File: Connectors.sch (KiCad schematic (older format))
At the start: 9 parts, among them J1 SM08B-CPTK-1A-TBL, J10 Conn_01x04, J17 Conn_01x04, J2 Conn_02x20_Odd_Even, J3 SM02B-CPTK-1A-TB, J5 BM02B-CPTK-1A-TB, J6 BM50B-SHLDS-G-TFT, J7 SM08B-CPTK-1A-TB, J8 BM08B-CPTK-1A-TB

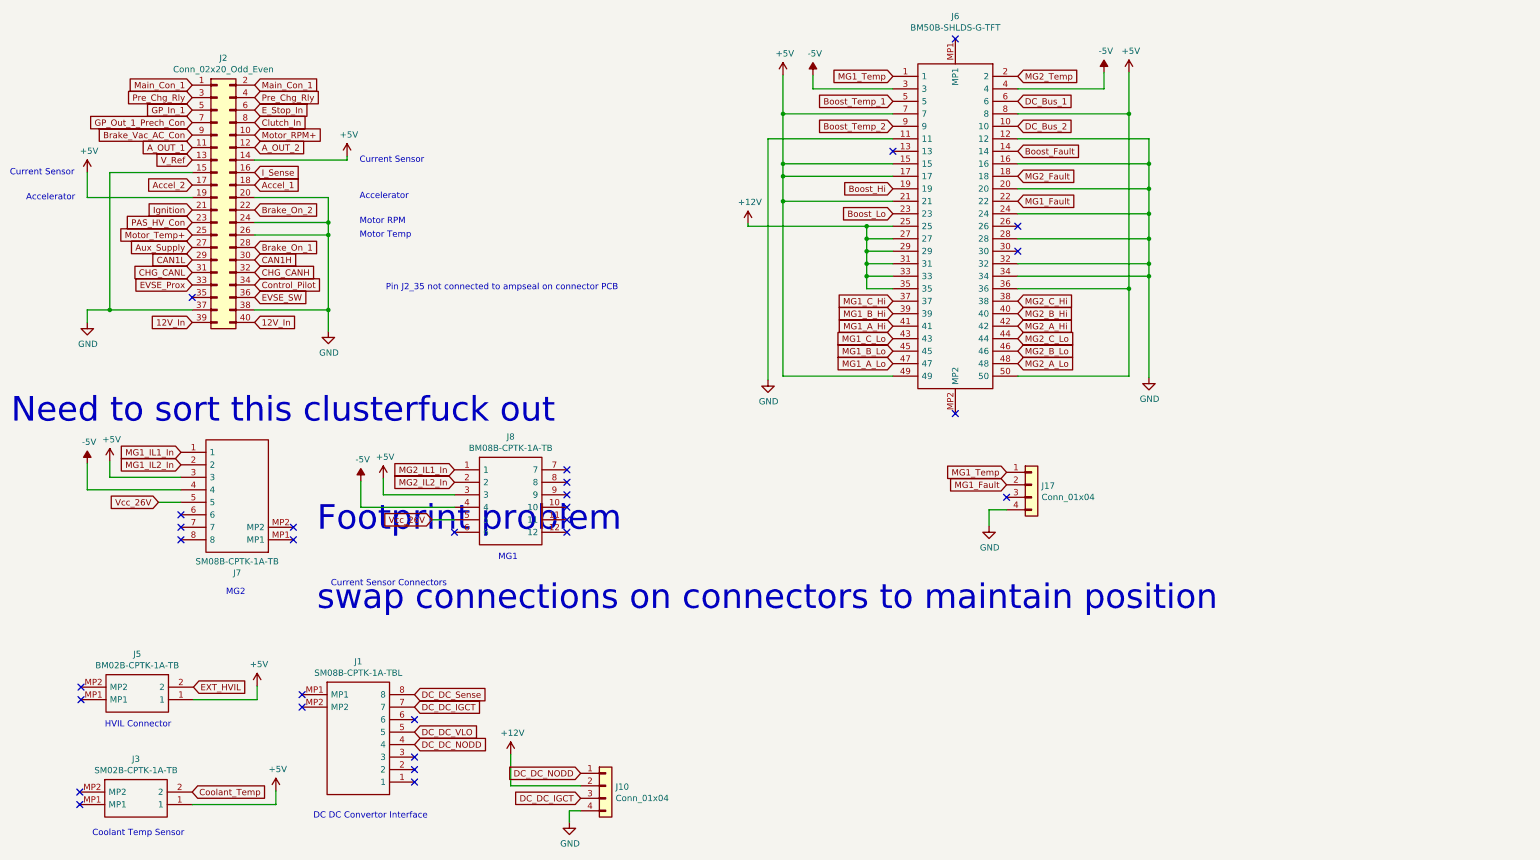
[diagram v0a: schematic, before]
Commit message: corrected tracking error around MG1 and MG current sensors.  J7 footprint updated (J1 left unchanged as tracking layout is currently ok).
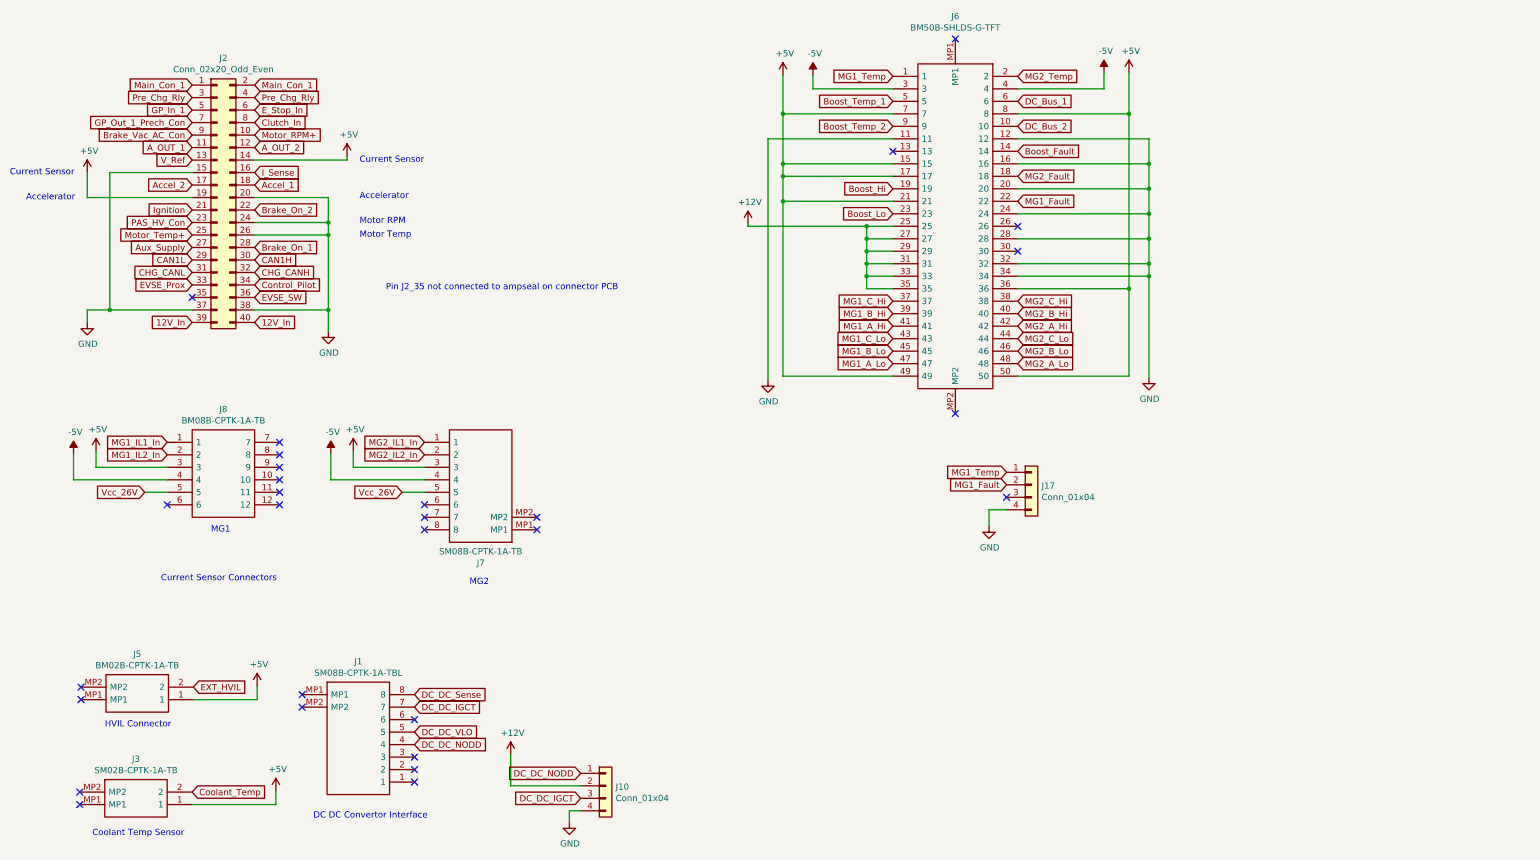
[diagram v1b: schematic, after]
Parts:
- J7: footprint SamacSys_Parts:SM08BCPTK1ATBL -> SamacSys_Parts:SM08BCPTK1ATBL_odd_even
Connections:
- net MG1_IL1_In: now also J8.1; no longer J7.1
- net MG1_IL2_In: now also J8.2; no longer J7.2
- net MG2_IL1_In: now also J7.1; no longer J8.1
- net MG2_IL2_In: now also J7.2; no longer J8.2
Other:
- note removed: "Footprint problem\n\nswap connections on connectors to maintain position"
- note removed: "Need to sort this clusterfuck out"
- moved on the sheet: J7, J8
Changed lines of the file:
@@
 Sheet 6 8
 Title "DC Controller STM32"
-Date "2020-07-04"
-Rev "2"
+Date "2020-10-18"
+Rev "3"
 Comp ""
 Comment1 "Designed: A Martell"
@@
 L SamacSys_Parts:SM08B-CPTK-1A-TBL J7
 U 1 1 5F32A5F1
-P 3060 4870
-F 0 "J7" H 3510 5135 50  0000 C CNN
-F 1 "SM08B-CPTK-1A-TB" H 3510 5044 50  0000 C CNN
-F 2 "SamacSys_Parts:SM08BCPTK1ATBL" H 3810 4970 50  0001 L CNN
-F 3 "http://www.jst-mfg.com/product/pdf/eng/eCPT.pdf" H 3810 4870 50  0001 L CNN
-F 4 "Header Top 8 Double CPT" H 3810 4770 50  0001 L CNN "Description"
-F 5 "12" H 3810 4670 50  0001 L CNN "Height"
-F 6 "" H 3810 4570 50  0001 L CNN "Mouser Part Number"
-F 7 "" H 3810 4470 50  0001 L CNN "Mouser Price/Stock"
-F 8 "JST (JAPAN SOLDERLESS TERMINALS)" H 3810 4370 50  0001 L CNN "Manufacturer_Name"
-F 9 "SM08B-CPTK-1A-TB" H 3810 4270 50  0001 L CNN "Manufacturer_Part_Number"
-	1    3060 4870
+P 5010 4790
+F 0 "J7" H 5460 5055 50  0000 C CNN
+F 1 "SM08B-CPTK-1A-TB" H 5460 4964 50  0000 C CNN
+F 2 "SamacSys_Parts:SM08BCPTK1ATBL_odd_even" H 5760 4890 50  0001 L CNN
+F 3 "http://www.jst-mfg.com/product/pdf/eng/eCPT.pdf" H 5760 4790 50  0001 L CNN
+F 4 "Header Top 8 Double CPT" H 5760 4690 50  0001 L CNN "Description"
+F 5 "12" H 5760 4590 50  0001 L CNN "Height"
+F 6 "" H 5760 4490 50  0001 L CNN "Mouser Part Number"
+F 7 "" H 5760 4390 50  0001 L CNN "Mouser Price/Stock"
+F 8 "JST (JAPAN SOLDERLESS TERMINALS)" H 5760 4290 50  0001 L CNN "Manufacturer_Name"
+F 9 "SM08B-CPTK-1A-TB" H 5760 4190 50  0001 L CNN "Manufacturer_Part_Number"
+	1    5010 4790
 	-1   0    0    1
 $EndComp
@@
 Text GLabel 2250 6890 2    50   Input ~ 0
 Coolant_Temp
-NoConn ~ 2160 4670
-NoConn ~ 3060 4870
-NoConn ~ 3060 4770
-NoConn ~ 2160 4870
-NoConn ~ 2160 4770
-NoConn ~ 4350 4810
-Text Notes 3360 5250 0    50   ~ 0
+NoConn ~ 4110 4590
+NoConn ~ 5010 4790
+NoConn ~ 5010 4690
+NoConn ~ 4110 4790
+NoConn ~ 4110 4690
+NoConn ~ 2050 4590
+Text Notes 2000 5210 0    50   ~ 0
 Current Sensor Connectors
 $Comp
@@
 Text GLabel 2250 2730 0    50   Input ~ 0
 CHG_CANL
-Text Notes 4700 5040 0    50   ~ 0
+Text Notes 2400 4820 0    50   ~ 0
 MG1
-Text Notes 2520 5320 0    50   ~ 0
+Text Notes 4470 5240 0    50   ~ 0
 MG2
-Text GLabel 2160 4170 0    50   Input ~ 0
+Text GLabel 2050 4090 0    50   Input ~ 0
 MG1_IL1_In
-Text GLabel 2160 4270 0    50   Input ~ 0
+Text GLabel 2050 4190 0    50   Input ~ 0
 MG1_IL2_In
 $Comp
 L power:+5V #PWR?
 U 1 1 5F14A7F7
-P 1590 4240
+P 3540 4160
 AR Path="/5F14A7F7" Ref="#PWR?"  Part="1"
 AR Path="/5EDFAF50/5F14A7F7" Ref="#PWR083"  Part="1"
-F 0 "#PWR083" H 1590 4090 50  0001 C CNN
-F 1 "+5V" H 1605 4413 50  0000 C CNN
-F 2 "" H 1590 4240 50  0001 C CNN
-F 3 "" H 1590 4240 50  0001 C CNN
-	1    1590 4240
+F 0 "#PWR083" H 3540 4010 50  0001 C CNN
+F 1 "+5V" H 3555 4333 50  0000 C CNN
+F 2 "" H 3540 4160 50  0001 C CNN
+F 3 "" H 3540 4160 50  0001 C CNN
+	1    3540 4160
 	1    0    0    -1
 $EndComp
@@
 L power:-5V #PWR?
 U 1 1 5F14DDA6
-P 1410 4260
+P 3360 4180
 AR Path="/5F8738CC/5F14DDA6" Ref="#PWR?"  Part="1"
 AR Path="/5EDFAF50/5F14DDA6" Ref="#PWR082"  Part="1"
-F 0 "#PWR082" H 1410 4360 50  0001 C CNN
-F 1 "-5V" H 1425 4433 50  0000 C CNN
-F 2 "" H 1410 4260 50  0001 C CNN
-F 3 "" H 1410 4260 50  0001 C CNN
-	1    1410 4260
-	1    0    0    -1
-$EndComp
-Text GLabel 1980 4570 0    50   Input ~ 0
+F 0 "#PWR082" H 3360 4280 50  0001 C CNN
+F 1 "-5V" H 3375 4353 50  0000 C CNN
+F 2 "" H 3360 4180 50  0001 C CNN
+F 3 "" H 3360 4180 50  0001 C CNN
+	1    3360 4180
+	1    0    0    -1
+$EndComp
+Text GLabel 3930 4490 0    50   Input ~ 0
 Vcc_26V
 Wire Wire Line
-	1980 4570 2160 4570
-Wire Wire Line
-	2160 4370 1590 4370
-Wire Wire Line
-	1590 4240 1590 4370
-Wire Wire Line
-	2160 4470 1410 4470
-Wire Wire Line
-	1410 4260 1410 4470
-Text GLabel 4350 4310 0    50   Input ~ 0
+	3930 4490 4110 4490
+Wire Wire Line
+	4110 4290 3540 4290
+Wire Wire Line
+	3540 4160 3540 4290
+Wire Wire Line
+	4110 4390 3360 4390
+Wire Wire Line
+	3360 4180 3360 4390
+Text GLabel 4110 4090 0    50   Input ~ 0
 MG2_IL1_In
-Text GLabel 4350 4410 0    50   Input ~ 0
+Text GLabel 4110 4190 0    50   Input ~ 0
 MG2_IL2_In
 $Comp
 L power:+5V #PWR?
 U 1 1 5F15B77F
-P 3780 4380
+P 1480 4160
 AR Path="/5F15B77F" Ref="#PWR?"  Part="1"
 AR Path="/5EDFAF50/5F15B77F" Ref="#PWR085"  Part="1"
-F 0 "#PWR085" H 3780 4230 50  0001 C CNN
-F 1 "+5V" H 3795 4553 50  0000 C CNN
-F 2 "" H 3780 4380 50  0001 C CNN
-F 3 "" H 3780 4380 50  0001 C CNN
-	1    3780 4380
+F 0 "#PWR085" H 1480 4010 50  0001 C CNN
+F 1 "+5V" H 1495 4333 50  0000 C CNN
+F 2 "" H 1480 4160 50  0001 C CNN
+F 3 "" H 1480 4160 50  0001 C CNN
+	1    1480 4160
 	1    0    0    -1
 $EndComp
@@
 L power:-5V #PWR?
 U 1 1 5F15B789
-P 3600 4400
+P 1300 4180
 AR Path="/5F8738CC/5F15B789" Ref="#PWR?"  Part="1"
 AR Path="/5EDFAF50/5F15B789" Ref="#PWR084"  Part="1"
-F 0 "#PWR084" H 3600 4500 50  0001 C CNN
-F 1 "-5V" H 3615 4573 50  0000 C CNN
-F 2 "" H 3600 4400 50  0001 C CNN
-F 3 "" H 3600 4400 50  0001 C CNN
-	1    3600 4400
-	1    0    0    -1
-$EndComp
-Text GLabel 4170 4710 0    50   Input ~ 0
+F 0 "#PWR084" H 1300 4280 50  0001 C CNN
+F 1 "-5V" H 1315 4353 50  0000 C CNN
+F 2 "" H 1300 4180 50  0001 C CNN
+F 3 "" H 1300 4180 50  0001 C CNN
+	1    1300 4180
+	1    0    0    -1
+$EndComp
+Text GLabel 1870 4490 0    50   Input ~ 0
 Vcc_26V
 Wire Wire Line
-	4170 4710 4350 4710
-Wire Wire Line
-	4350 4510 3780 4510
-Wire Wire Line
-	3780 4380 3780 4510
-Wire Wire Line
-	4350 4610 3600 4610
-Wire Wire Line
-	3600 4400 3600 4610
+	1870 4490 2050 4490
+Wire Wire Line
+	2050 4290 1480 4290
+Wire Wire Line
+	1480 4160 1480 4290
+Wire Wire Line
+	2050 4390 1300 4390
+Wire Wire Line
+	1300 4180 1300 4390
 Text GLabel 2750 1430 2    50   Input ~ 0
 E_Stop_In
@@
 Text GLabel 2750 2830 2    50   Input ~ 0
 Control_Pilot
-NoConn ~ 5250 4510
-NoConn ~ 5250 4610
-NoConn ~ 5250 4710
-NoConn ~ 5250 4810
-NoConn ~ 5250 4410
-NoConn ~ 5250 4310
+NoConn ~ 2950 4290
+NoConn ~ 2950 4390
+NoConn ~ 2950 4490
+NoConn ~ 2950 4590
+NoConn ~ 2950 4190
+NoConn ~ 2950 4090
 $Comp
 L SamacSys_Parts:BM08B-CPTK-1A-TB J8
 U 1 1 5F32A8B6
-P 4350 4310
-F 0 "J8" H 4800 4575 50  0000 C CNN
-F 1 "BM08B-CPTK-1A-TB" H 4800 4484 50  0000 C CNN
-F 2 "SamacSys_Parts:BM08BCPTK1ATB" H 5100 4410 50  0001 L CNN
-F 3 "http://www.jst-mfg.com/product/pdf/eng/eCPT.pdf" H 5100 4310 50  0001 L CNN
-F 4 "Header Top 8 Double CPT" H 5100 4210 50  0001 L CNN "Description"
-F 5 "12" H 5100 4110 50  0001 L CNN "Height"
-F 6 "306-BM08B-CPTK-1A-TB" H 5100 4010 50  0001 L CNN "Mouser Part Number"
-F 7 "https://www.mouser.co.uk/ProductDetail/JST-Automotive/BM08B-CPTK-1A-TB?qs=XoGB3caz5%2FYvSzPNYjsAKw%3D%3D" H 5100 3910 50  0001 L CNN "Mouser Price/Stock"
-F 8 "JST (JAPAN SOLDERLESS TERMINALS)" H 5100 3810 50  0001 L CNN "Manufacturer_Name"
-F 9 "BM08B-CPTK-1A-TB" H 5100 3710 50  0001 L CNN "Manufacturer_Part_Number"
-	1    4350 4310
-	1    0    0    -1
-$EndComp
-Text Notes 800  3950 0    197  ~ 0
-Need to sort this clusterfuck out
-Text Notes 3250 5450 0    197  ~ 0
-Footprint problem\n\nswap connections on connectors to maintain position
+P 2050 4090
+F 0 "J8" H 2500 4355 50  0000 C CNN
+F 1 "BM08B-CPTK-1A-TB" H 2500 4264 50  0000 C CNN
+F 2 "SamacSys_Parts:BM08BCPTK1ATB" H 2800 4190 50  0001 L CNN
+F 3 "http://www.jst-mfg.com/product/pdf/eng/eCPT.pdf" H 2800 4090 50  0001 L CNN
+F 4 "Header Top 8 Double CPT" H 2800 3990 50  0001 L CNN "Description"
+F 5 "12" H 2800 3890 50  0001 L CNN "Height"
+F 6 "306-BM08B-CPTK-1A-TB" H 2800 3790 50  0001 L CNN "Mouser Part Number"
+F 7 "https://www.mouser.co.uk/ProductDetail/JST-Automotive/BM08B-CPTK-1A-TB?qs=XoGB3caz5%2FYvSzPNYjsAKw%3D%3D" H 2800 3690 50  0001 L CNN "Mouser Price/Stock"
+F 8 "JST (JAPAN SOLDERLESS TERMINALS)" H 2800 3590 50  0001 L CNN "Manufacturer_Name"
+F 9 "BM08B-CPTK-1A-TB" H 2800 3490 50  0001 L CNN "Manufacturer_Part_Number"
+	1    2050 4090
+	1    0    0    -1
+$EndComp
 $EndSCHEMATC
